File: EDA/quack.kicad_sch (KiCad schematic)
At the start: 17 parts, among them U1 AMS1117-3.3, U3 ESP32-PICO-V3

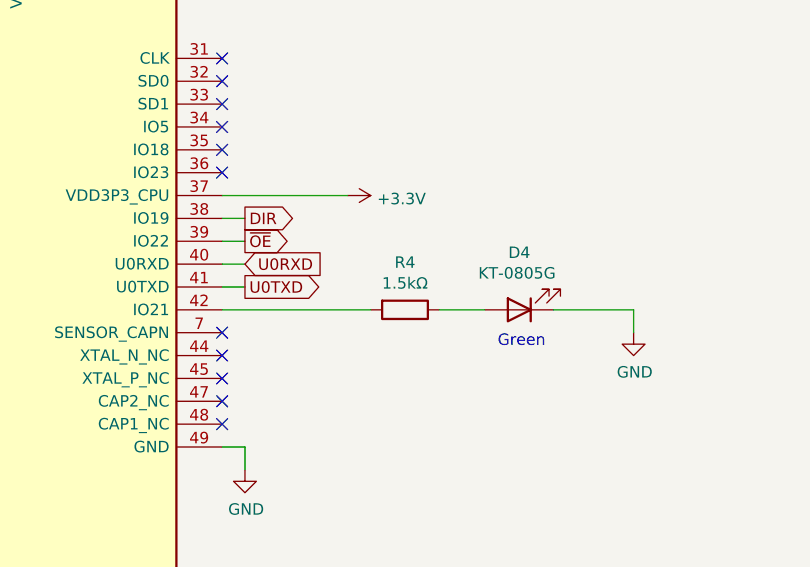
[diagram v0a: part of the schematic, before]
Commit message: bump emerald LED from 1.5kΩ to 2.2kΩ
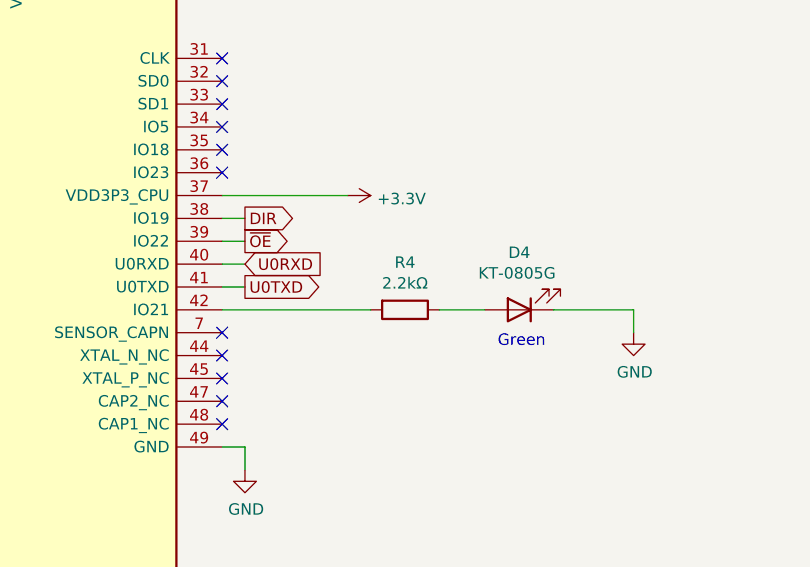
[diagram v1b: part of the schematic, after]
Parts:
- R4: value 1.5kΩ -> 2.2kΩ
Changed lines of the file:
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@@
 			)
 		)
-		(property "Value" "1.5kΩ"
+		(property "Value" "2.2kΩ"
 			(at 171.45 98.6536 90)
 			(effects
